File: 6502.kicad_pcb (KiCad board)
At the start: 2 copper layers, 95.2 x 95.3 mm, 38 parts, among them J3 Conn_01x40, J4 CPU Control, SW1 Reset, U1 W65C02SxP, U2 AT28C256, U3 HM62256BLP, Y1 1MHz

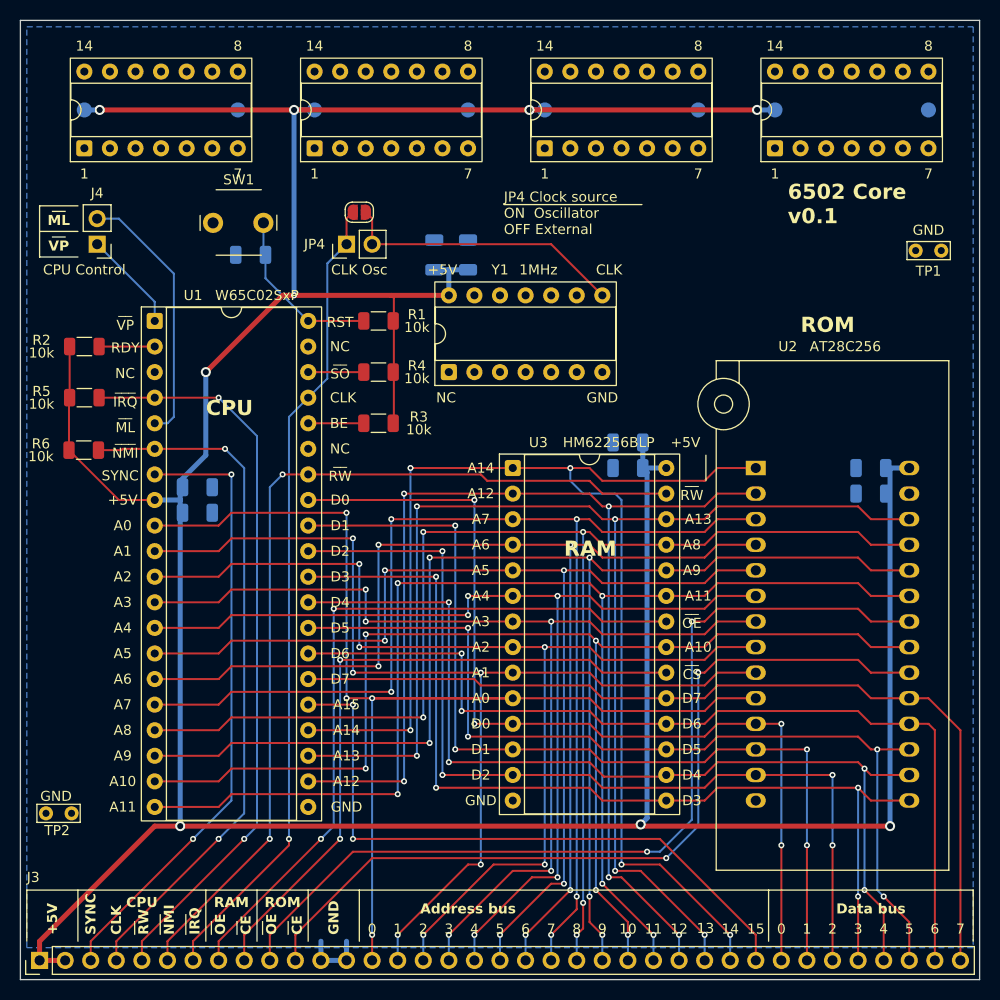
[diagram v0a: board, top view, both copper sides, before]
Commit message: 6502.kicad_pro: Fix a few post-production issues
Fixed a few issues found on the v0.1 boards:

- J3: Fix misplaced CLK/RW/NMI/IRQ CPU labels
- J3: Fix CE->CS for both RAM and ROM
- J3: Move via next to A0 for more solid BG ground polygon
- J4: Reroute on the front for more solid BG ground polygon
- RAM: Move vias out of OE and CS F.silk
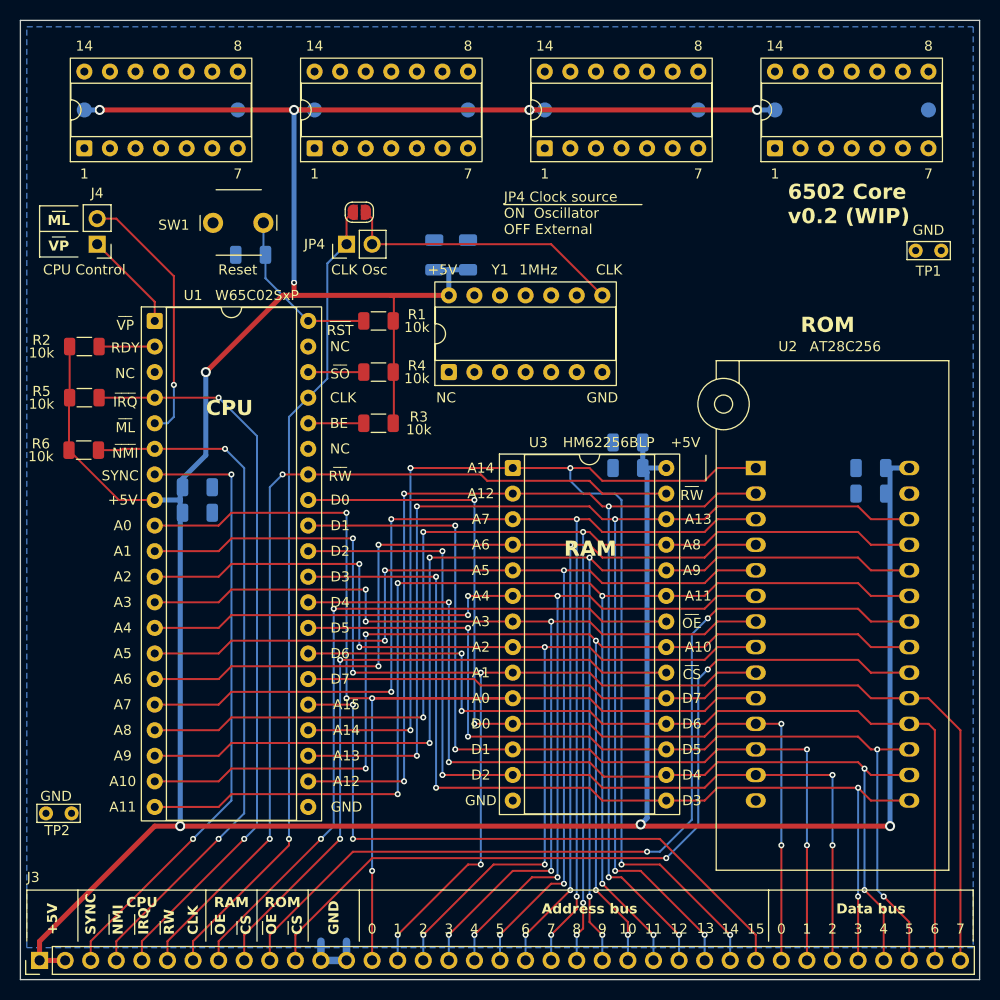
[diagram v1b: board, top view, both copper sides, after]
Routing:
- net ROM_OEB: track 91.5 -> 90.8 mm
- net CPU_MLB: track 26.3 -> 26.1 mm, vias 0 -> 1
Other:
- board text added: "6502 Core v0.2 (WIP)"
- board text added: "___ RST"
- board text removed: "6502 Core v0.1"
- board text removed: "RST"
- board text removed: "__ CE"
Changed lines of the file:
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@@
 		(tags "tact sw push 6mm")
 		(property "Reference" "SW1"
-			(at 0.0496 -4.2888 0)
+			(at -6.39 0.215 0)
 			(layer "F.SilkS")
 			(effects
@@
 		)
 		(property "Value" "Reset"
-			(at 0.5496 4.4112 0)
-			(layer "F.Fab")
+			(at -0.04 4.66 0)
+			(layer "F.SilkS")
 			(effects
 				(font
@@
 	)
 	(gr_text "___\nNMI"
-		(at 73.66 169.545 90)
+		(at 68.58 169.545 90)
 		(layer "F.SilkS")
 		(effects
@@
 	)
 	(gr_text "___\nIRQ"
-		(at 76.2 169.545 90)
+		(at 71.12 169.545 90)
 		(layer "F.SilkS")
 		(effects
@@
 		)
 	)
-	(gr_text "__\nCE"
+	(gr_text "__\nCS"
 		(at 86.36 169.545 90)
 		(layer "F.SilkS")
@@
 		)
 	)
-	(gr_text "RST"
+	(gr_text "___\nRST"
 		(at 91.44 108.712 0)
 		(layer "F.SilkS")
@@
 		)
 	)
-	(gr_text "__\nCE"
+	(gr_text "__\nCS"
 		(at 81.28 169.545 90)
 		(layer "F.SilkS")
@@
 	)
 	(gr_text "Address bus"
-		(at 104.14 166.37 0)
+		(at 116.205 166.37 0)
 		(layer "F.SilkS")
 		(effects
@@
 		)
 	)
-	(gr_text "6502 Core\nv0.1\n"
+	(gr_text "6502 Core\nv0.2 (WIP)\n"
 		(at 135.89 99.06 0)
 		(layer "F.SilkS")
@@
 	)
 	(gr_text "__\nRW"
-		(at 71.12 169.545 90)
+		(at 73.66 169.545 90)
 		(layer "F.SilkS")
 		(effects
@@
 	)
 	(gr_text "CLK"
-		(at 69.215 169.545 90)
+		(at 76.835 169.545 90)
 		(layer "F.SilkS")
 		(effects
@@
 	)
 	(segment
-		(start 96.774 113.6035)
-		(end 96.7125 113.665)
-		(width 0.2)
+		(start 86.868 104.775)
+		(end 86.868 106.045)
+		(width 0.5)
 		(layer "F.Cu")
 		(net 2)
 	)
 	(segment
-		(start 96.52 106.045)
-		(end 86.868 106.045)
-		(width 0.5)
+		(start 96.774 113.6035)
+		(end 96.7125 113.665)
+		(width 0.2)
 		(layer "F.Cu")
 		(net 2)
@@
 	)
 	(segment
+		(start 85.725 106.045)
+		(end 78.105 113.665)
+		(width 0.5)
+		(layer "F.Cu")
+		(net 2)
+	)
+	(segment
 		(start 69.469 126.365)
 		(end 64.516 121.412)
@@
 	)
 	(segment
+		(start 86.868 106.045)
+		(end 85.725 106.045)
+		(width 0.5)
+		(layer "F.Cu")
+		(net 2)
+	)
+	(segment
 		(start 61.595 172.085)
 		(end 64.135 172.085)
@@
 	)
 	(segment
-		(start 85.725 106.045)
-		(end 78.105 113.665)
-		(width 0.5)
-		(layer "F.Cu")
-		(net 2)
-	)
-	(segment
 		(start 73.03 126.365)
 		(end 69.469 126.365)
@@
 	)
 	(segment
-		(start 61.595 170.18)
-		(end 61.595 172.085)
+		(start 96.52 106.045)
+		(end 86.868 106.045)
 		(width 0.5)
 		(layer "F.Cu")
@@
 	)
 	(segment
-		(start 86.868 106.045)
-		(end 85.725 106.045)
+		(start 61.595 170.18)
+		(end 61.595 172.085)
 		(width 0.5)
 		(layer "F.Cu")
@@
 	)
 	(via
-		(at 86.868 106.045)
+		(at 86.868 104.775)
 		(size 0.6)
 		(drill 0.3)
@@
 	)
 	(segment
+		(start 86.868 104.775)
+		(end 86.868 87.63)
+		(width 0.5)
+		(layer "B.Cu")
+		(net 2)
+	)
+	(segment
 		(start 121.92 157.95)
 		(end 121.92 123.62)
@@
 	)
 	(segment
-		(start 86.868 106.045)
-		(end 86.868 87.63)
-		(width 0.5)
-		(layer "B.Cu")
-		(net 2)
-	)
-	(segment
 		(start 117.475 147.32)
 		(end 127.635 147.32)
@@
 	(segment
 		(start 94.615 172.085)
-		(end 94.615 169.545)
+		(end 94.615 163.195)
 		(width 0.2)
 		(layer "F.Cu")
@@
 	)
 	(via
-		(at 94.615 169.545)
+		(at 94.615 163.195)
 		(size 0.6)
 		(drill 0.3)
@@
 	(segment
 		(start 94.615 146.05)
-		(end 94.615 169.545)
+		(end 94.615 163.195)
 		(width 0.2)
 		(layer "B.Cu")
@@
 		(start 89.535 172.085)
 		(end 89.535 170.18)
-		(width 0.5)
+		(width 0.75)
 		(layer "B.Cu")
 		(net 9)
@@
 		(start 92.075 172.085)
 		(end 92.075 170.18)
-		(width 0.5)
+		(width 0.75)
 		(layer "B.Cu")
 		(net 9)
@@
 		(start 92.075 172.085)
 		(end 89.535 172.085)
-		(width 0.5)
+		(width 0.75)
 		(layer "B.Cu")
 		(net 9)
@@
 	)
 	(segment
-		(start 69.469 98.425)
-		(end 67.31 98.425)
+		(start 74.93 104.14)
+		(end 69.215 98.425)
 		(width 0.2)
-		(layer "B.Cu")
+		(layer "F.Cu")
 		(net 39)
 	)
 	(segment
-		(start 74.295 118.745)
-		(end 74.93 118.11)
+		(start 74.93 114.935)
+		(end 74.93 104.14)
 		(width 0.2)
-		(layer "B.Cu")
+		(layer "F.Cu")
 		(net 39)
 	)
 	(segment
-		(start 73.03 118.745)
-		(end 74.295 118.745)
+		(start 69.215 98.425)
+		(end 67.31 98.425)
 		(width 0.2)
-		(layer "B.Cu")
+		(layer "F.Cu")
+		(net 39)
+	)
+	(via
+		(at 74.93 114.935)
+		(size 0.6)
+		(drill 0.3)
+		(layers "F.Cu" "B.Cu")
 		(net 39)
 	)
 	(segment
-		(start 74.93 103.886)
-		(end 69.469 98.425)
+		(start 74.93 118.11)
+		(end 74.295 118.745)
 		(width 0.2)
 		(layer "B.Cu")
@@
 	)
 	(segment
-		(start 74.93 118.11)
-		(end 74.93 103.886)
+		(start 74.295 118.745)
+		(end 73.03 118.745)
 		(width 0.2)
 		(layer "B.Cu")
@@
 	)
 	(segment
-		(start 127.635 143.51)
-		(end 127 143.51)
+		(start 74.93 114.935)
+		(end 74.93 118.11)
 		(width 0.2)
-		(layer "F.Cu")
-		(net 40)
+		(layer "B.Cu")
+		(net 39)
 	)
 	(segment
-		(start 144.145 143.51)
-		(end 142.875 142.24)
+		(start 127.9525 143.1925)
+		(end 128.905 142.24)
 		(width 0.2)
 		(layer "F.Cu")
@@
 	)
 	(segment
-		(start 142.875 142.24)
-		(end 128.905 142.24)
+		(start 94.615 161.925)
+		(end 86.995 169.545)
 		(width 0.2)
 		(layer "F.Cu")
@@
 	)
 	(segment
-		(start 94.615 161.925)
-		(end 86.995 169.545)
+		(start 128.905 142.24)
+		(end 142.875 142.24)
 		(width 0.2)
 		(layer "F.Cu")
@@
 	)
 	(segment
-		(start 147.955 143.51)
+		(start 142.875 142.24)
 		(end 144.145 143.51)
 		(width 0.2)
@@
 	)
 	(segment
-		(start 128.905 142.24)
-		(end 127.635 143.51)
+		(start 144.145 143.51)
+		(end 147.955 143.51)
 		(width 0.2)
 		(layer "F.Cu")
@@
 	)
 	(via
-		(at 127 143.51)
+		(at 127.9525 143.1925)
 		(size 0.6)
 		(drill 0.3)
@@
 	)
 	(segment
+		(start 127 144.145)
+		(end 127 158.75)
+		(width 0.2)
+		(layer "B.Cu")
+		(net 40)
+	)
+	(segment
 		(start 127 158.75)
-		(end 127 143.51)
+		(end 123.825 161.925)
 		(width 0.2)
 		(layer "B.Cu")
@@
 	)
 	(segment
-		(start 123.825 161.925)
-		(end 127 158.75)
+		(start 127.9525 143.1925)
+		(end 127 144.145)
 		(width 0.2)
 		(layer "B.Cu")
@@
 	)
 	(segment
+		(start 142.875 137.16)
+		(end 144.145 138.43)
+		(width 0.2)
+		(layer "F.Cu")
+		(net 42)
+	)
+	(segment
 		(start 144.145 138.43)
-		(end 142.875 137.16)
+		(end 147.955 138.43)
 		(width 0.2)
 		(layer "F.Cu")
@@
 	)
 	(segment
-		(start 142.875 137.16)
-		(end 128.905 137.16)
+		(start 128.905 137.16)
+		(end 142.875 137.16)
 		(width 0.2)
 		(layer "F.Cu")
@@
 	)
 	(segment
-		(start 147.955 138.43)
-		(end 144.145 138.43)
+		(start 127.9525 138.1125)
+		(end 128.905 137.16)
 		(width 0.2)
 		(layer "F.Cu")
@@
 		(net 42)
 	)
-	(segment
-		(start 128.905 137.16)
-		(end 127.635 138.43)
-		(width 0.2)
-		(layer "F.Cu")
-		(net 42)
-	)
-	(segment
-		(start 127.635 138.43)
-		(end 126.365 138.43)
-		(width 0.2)
-		(layer "F.Cu")
-		(net 42)
-	)
 	(via
-		(at 126.365 138.43)
+		(at 127.9525 138.1125)
 		(size 0.6)
 		(drill 0.3)
@@
 	)
 	(segment
-		(start 126.365 158.115)
-		(end 126.365 138.43)
+		(start 127.9525 138.1125)
+		(end 126.365 139.7)
 		(width 0.2)
 		(layer "B.Cu")
@@
 	)
 	(segment
-		(start 121.92 161.29)
-		(end 123.19 161.29)
+		(start 126.365 139.7)
+		(end 126.365 158.115)
 		(width 0.2)
 		(layer "B.Cu")
@@
 	(segment
 		(start 123.19 161.29)
-		(end 126.365 158.115)
+		(end 121.92 161.29)
 		(width 0.2)
 		(layer "B.Cu")
@@
 	)
 	(segment
-		(start 73.03 108.585)
-		(end 73.03 106.685)
+		(start 126.365 158.115)
+		(end 123.19 161.29)
 		(width 0.2)
 		(layer "B.Cu")
-		(net 43)
+		(net 42)
 	)
 	(segment
 		(start 73.03 106.685)
-		(end 67.31 100.965)
+		(end 73.03 108.585)
 		(width 0.2)
-		(layer "B.Cu")
+		(layer "F.Cu")
+		(net 43)
+	)
+	(segment
+		(start 67.31 100.965)
+		(end 73.03 106.685)
+		(width 0.2)
+		(layer "F.Cu")
 		(net 43)
 	)

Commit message: Update schematics
Schematics:

- J3: Replace SYNC with RST
- J4: Add SYNC
- Rename CEB do CSB (Chip Enabled -> Chip Select)

PCB:
- Increase GND Polygon min clearance
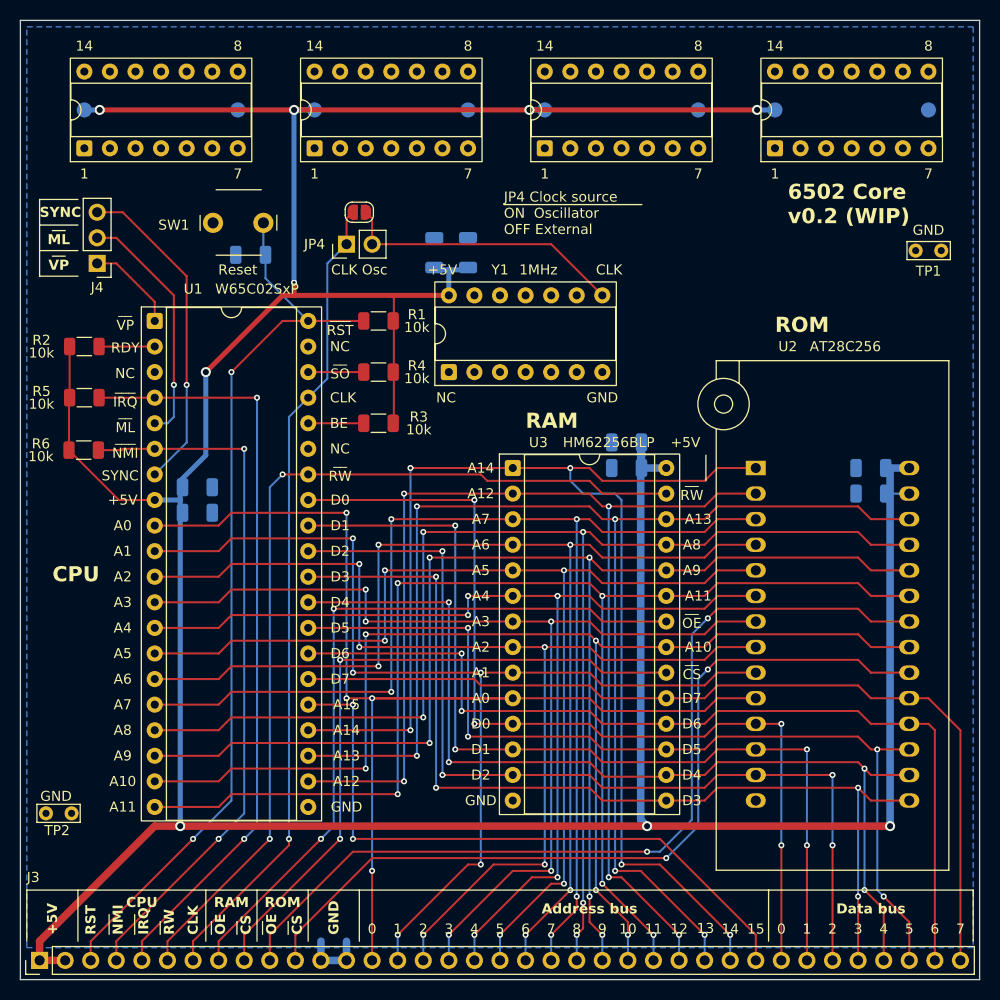
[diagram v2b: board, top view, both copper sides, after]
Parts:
- J4: footprint Connector_PinHeader_2.54mm:PinHeader_1x02_P2.54mm_Vertical -> Connector_PinHeader_2.54mm:PinHeader_1x03_P2.54mm_Vertical
- moved J4 1.91 mm to (67.3, 102.9)
- moved C8 0.22 mm to (104.1, 101.8)
- moved C9 0.22 mm to (100.8, 101.8)
- moved C3 0.13 mm to (119.9, 123.2)
- moved C6 0.13 mm to (119.9, 120.7)
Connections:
- net ROM_CEB renamed ROM_CSB
- J3 pad 3: CPU_SYNC -> RESET
- U2 pad 27: unconnected-(U2-WEB-Pad27) -> +5V
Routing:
- net RESET: track 17.1 -> 91.0 mm, vias 0 -> 2
- net CPU_SYNC: track 61.7 -> 32.5 mm, vias 2 -> 1
- net +5V: track 378.1 -> 383.0 mm
- net CPU_IRQ: track 74.1 -> 76.3 mm
- net CPU_MLB: track 26.1 -> 24.2 mm
- net CPU_NMI: track 69.5 -> 70.6 mm
- net CPU_VPB: track 9.99 -> 9.20 mm
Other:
- board text added: "RST"
